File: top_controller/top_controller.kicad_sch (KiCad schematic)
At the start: 117 parts, among them J1 OUT1, J10 USB_C_Receptacle_USB2.0, J11 SWD, J12 UART, J13 BOOT0, J14 BOOT1, J2 OUT2, J3 OUT3, J4 OUT4, J5 OUT5, J6 OUT6, J7 OUT7, J8 OUT8, J9 PIN, SW1 RESET, U1 STM32F103C8Tx, U2 LT3045xMSE, U3 AD5754BREZ, U4 AD5754BREZ, U5 REF192, U6 EPM78V2, U7 REF192, Y1 8MHz

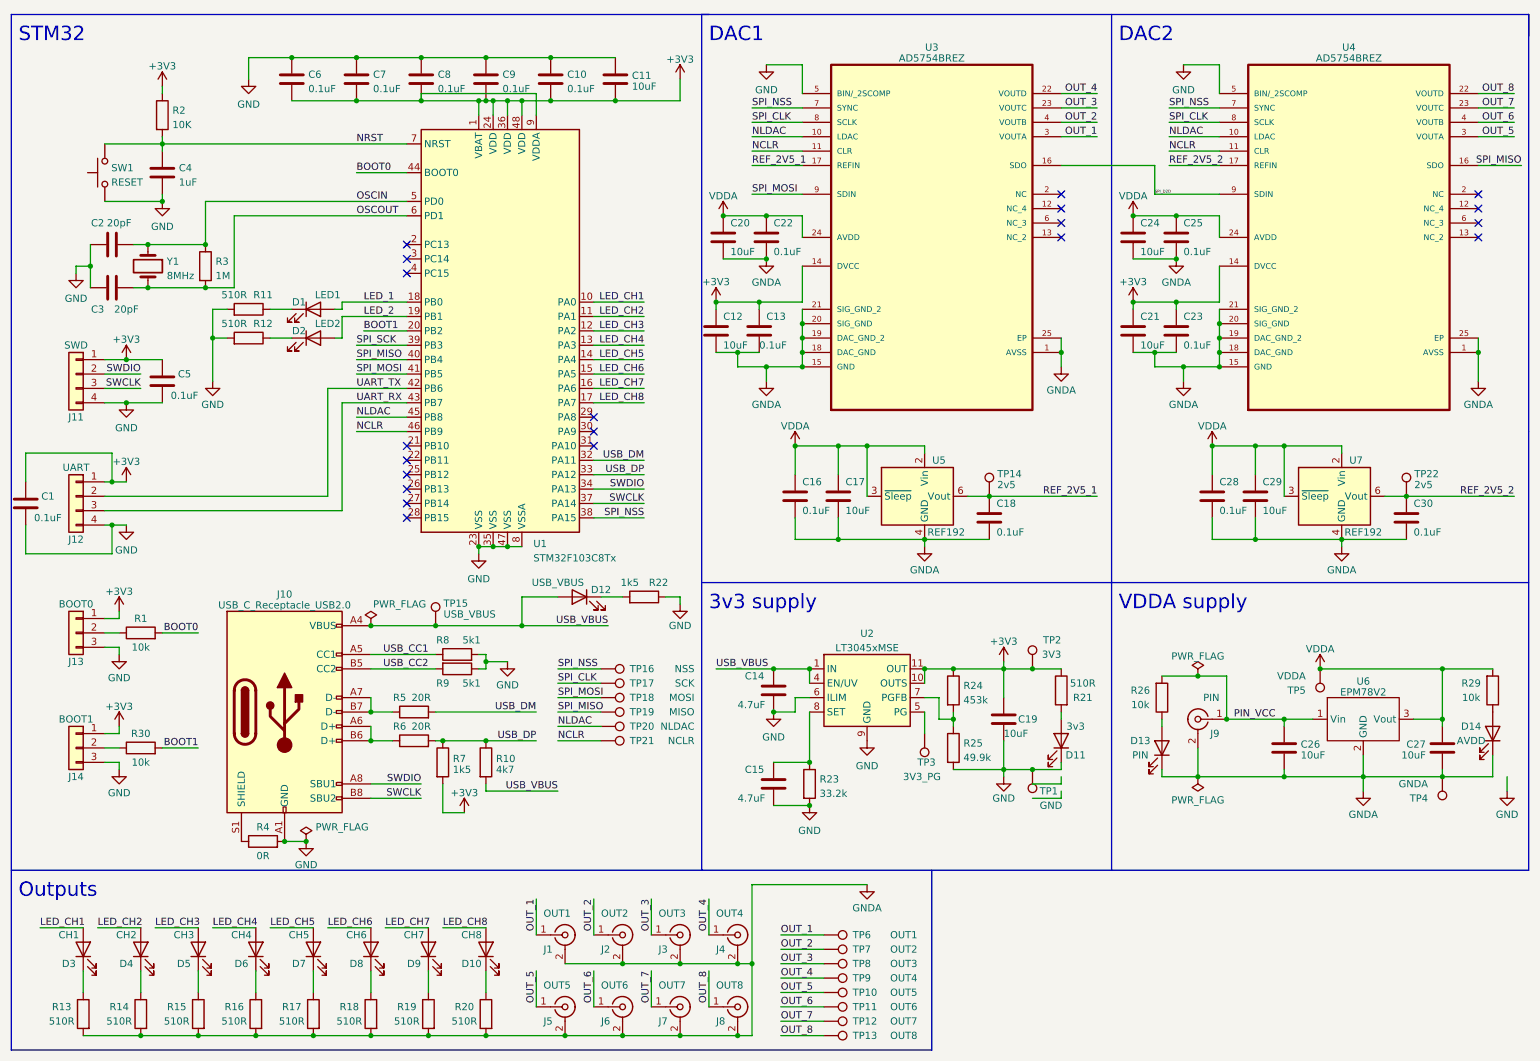
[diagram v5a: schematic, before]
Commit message: Reordered output channels on DACs for easier tracing
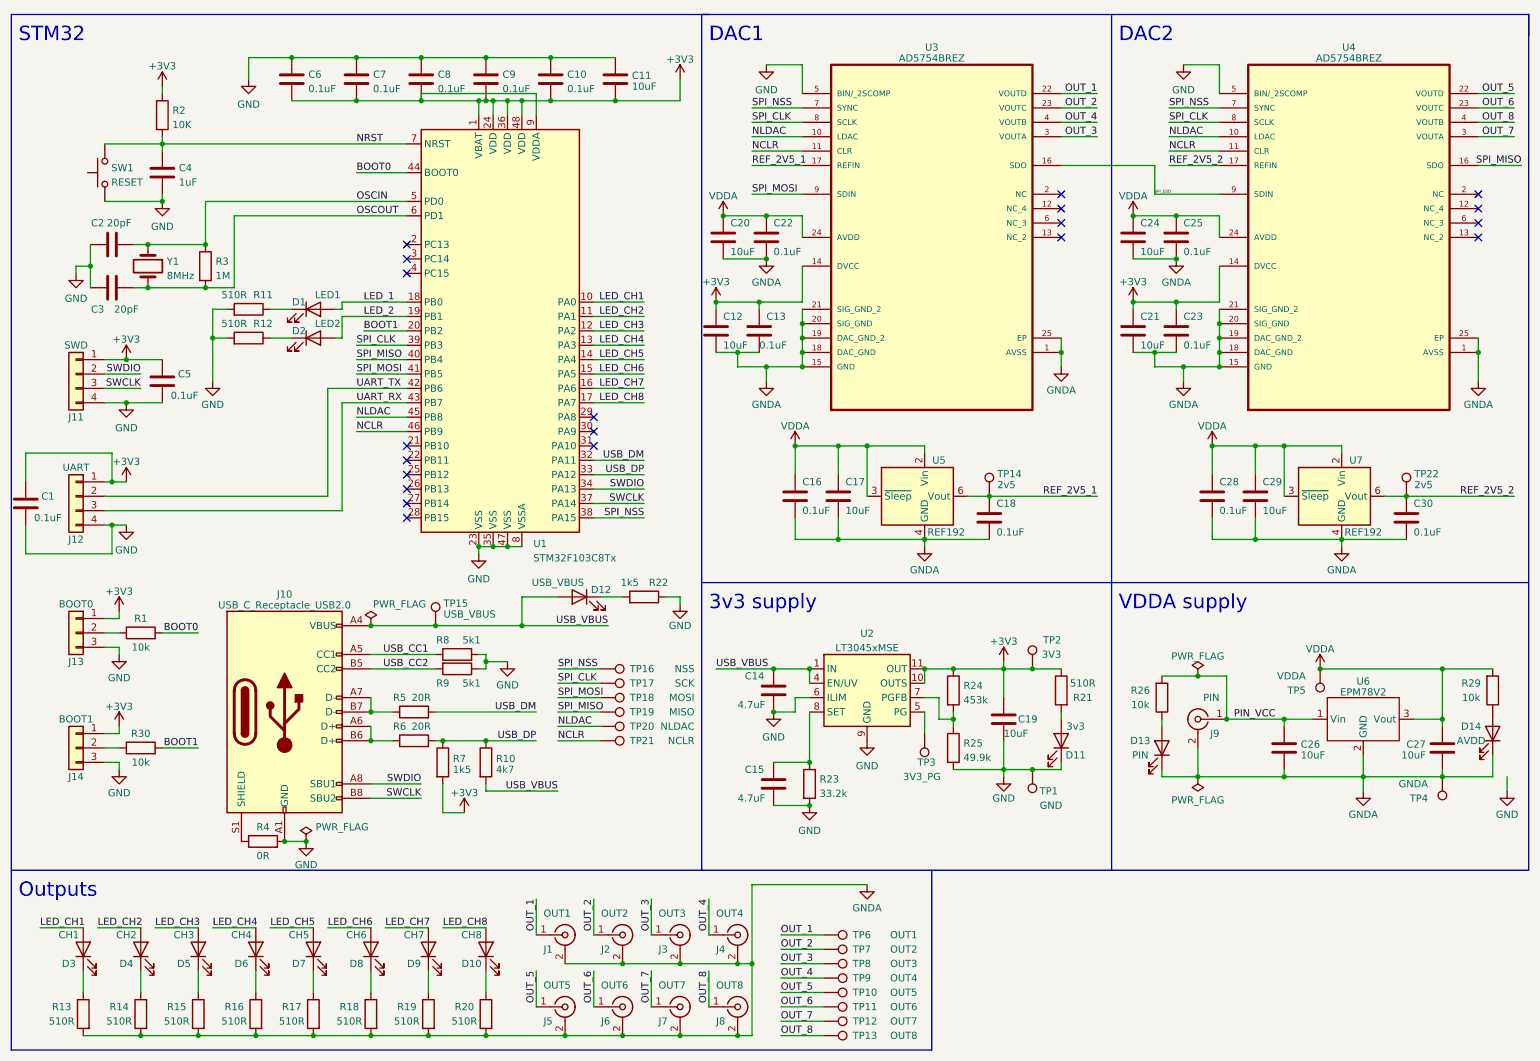
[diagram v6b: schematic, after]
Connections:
- net SPI_SCK is gone; now on net SPI_CLK: U1.39 (PB3)
- net OUT_1: now also U3.22 (VOUTD); no longer U3.3 (VOUTA)
- net OUT_2: now also U3.23 (VOUTC); no longer U3.4 (VOUTB)
- net OUT_3: now also U3.3 (VOUTA); no longer U3.23 (VOUTC)
- net OUT_4: now also U3.4 (VOUTB); no longer U3.22 (VOUTD)
- net OUT_5: now also U4.22 (VOUTD); no longer U4.3 (VOUTA)
- net OUT_6: now also U4.23 (VOUTC); no longer U4.4 (VOUTB)
- net OUT_7: now also U4.3 (VOUTA); no longer U4.23 (VOUTC)
- net OUT_8: now also U4.4 (VOUTB); no longer U4.22 (VOUTD)
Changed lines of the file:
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@@
-    (stroke (width 0) (type default))
-  )
-  (wire (pts (xy 199.39 149.86) (xy 194.31 149.86))
     (stroke (width 0) (type default))
   )
@@
     (stroke (width 0) (type default))
   )
-  (wire (pts (xy 199.39 152.4) (xy 194.31 152.4))
-    (stroke (width 0) (type default))
-  )
   (wire (pts (xy 199.39 71.12) (xy 199.39 73.66))
     (stroke (width 0) (type default))
@@
     (stroke (width 0) (type default))
   )
-  (wire (pts (xy 199.39 148.59) (xy 199.39 149.86))
-    (stroke (width 0) (type default))
-  )
   (wire (pts (xy 226.06 106.68) (xy 226.06 102.87))
     (stroke (width 0) (type default))
@@
     (stroke (width 0) (type default))
   )
-  (wire (pts (xy 199.39 151.13) (xy 199.39 152.4))
-    (stroke (width 0) (type default))
-  )
   (wire (pts (xy 149.86 191.77) (xy 157.48 191.77))
     (stroke (width 0) (type default))
@@
     (effects (font (size 1.27 1.27)) (justify right bottom))
   )
-  (label "OUT_1" (at 205.74 35.56 180) (fields_autoplaced)
+  (label "OUT_3" (at 205.74 35.56 180) (fields_autoplaced)
     (effects (font (size 1.27 1.27)) (justify right bottom))
   )
@@
     (effects (font (size 1.27 1.27)) (justify right bottom))
   )
-  (label "OUT_8" (at 279.4 27.94 180) (fields_autoplaced)
+  (label "OUT_5" (at 279.4 27.94 180) (fields_autoplaced)
     (effects (font (size 1.27 1.27)) (justify right bottom))
   )
@@
     (effects (font (size 1.27 1.27)) (justify left bottom))
   )
-  (label "OUT_7" (at 279.4 30.48 180) (fields_autoplaced)
+  (label "OUT_6" (at 279.4 30.48 180) (fields_autoplaced)
     (effects (font (size 1.27 1.27)) (justify right bottom))
   )
@@
     (effects (font (size 1.27 1.27)) (justify right bottom))
   )
-  (label "OUT_3" (at 205.74 30.48 180) (fields_autoplaced)
+  (label "OUT_2" (at 205.74 30.48 180) (fields_autoplaced)
     (effects (font (size 1.27 1.27)) (justify right bottom))
   )
@@
     (effects (font (size 1.27 1.27)) (justify left bottom))
   )
-  (label "SPI_SCK" (at 74.93 72.39 0) (fields_autoplaced)
-    (effects (font (size 1.27 1.27)) (justify left bottom))
-  )
-  (label "OUT_2" (at 205.74 33.02 180) (fields_autoplaced)
-    (effects (font (size 1.27 1.27)) (justify right bottom))
-  )
-  (label "OUT_4" (at 205.74 27.94 180) (fields_autoplaced)
+  (label "SPI_CLK" (at 74.93 72.39 0) (fields_autoplaced)
+    (effects (font (size 1.27 1.27)) (justify left bottom))
+  )
+  (label "OUT_4" (at 205.74 33.02 180) (fields_autoplaced)
+    (effects (font (size 1.27 1.27)) (justify right bottom))
+  )
+  (label "OUT_1" (at 205.74 27.94 180) (fields_autoplaced)
     (effects (font (size 1.27 1.27)) (justify right bottom))
   )
@@
     (effects (font (size 1.27 1.27)) (justify right bottom))
   )
-  (label "OUT_5" (at 279.4 35.56 180) (fields_autoplaced)
+  (label "OUT_7" (at 279.4 35.56 180) (fields_autoplaced)
     (effects (font (size 1.27 1.27)) (justify right bottom))
   )
@@
     (effects (font (size 1.27 1.27)) (justify left bottom))
   )
-  (label "OUT_6" (at 279.4 33.02 180) (fields_autoplaced)
-    (effects (font (size 1.27 1.27)) (justify right bottom))
-  )
+  (label "OUT_8" (at 279.4 33.02 180) (fields_autoplaced)
+    (effects (font (size 1.27 1.27)) (justify right bottom))
+  )

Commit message: Finished tracing - still some errors present
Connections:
- net GNDA is gone; now on net GND: C12.2, C13.2, C16.2, C17.2, C18.2, C20.2, C21.2, C22.2, C23.2, C24.2, C25.2, C26.2, C27.2, C28.2, C29.2, C30.2, D13.1 (K), D14.1 (K), J1.2 (Ext), J2.2 (Ext), J3.2 (Ext), J4.2 (Ext), J5.2 (Ext), J6.2 (Ext), J7.2 (Ext), J8.2 (Ext), J9.2 (Ext), R13.2, R14.2, R15.2, R16.2, R17.2, R18.2, R19.2, R20.2, TP4.1, U3.1 (AVSS), U3.15 (GND), U3.18 (DAC_GND), U3.19 (DAC_GND_2), U3.20 (SIG_GND), U3.21 (SIG_GND_2), U3.25 (EP), U4.1 (AVSS), U4.15 (GND), U4.18 (DAC_GND), U4.19 (DAC_GND_2), U4.20 (SIG_GND), U4.21 (SIG_GND_2), U4.25 (EP), U5.4 (GND), U6.2 (GND), U7.4 (GND)
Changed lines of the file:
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@@
   (junction (at 138.43 64.77) (diameter 0) (color 0 0 0 0)
+  )
+  (junction (at 275.59 148.59) (diameter 0) (color 0 0 0 0)
   )
   (junction (at 111.76 194.31) (diameter 0) (color 0 0 0 0)
@@
     (stroke (width 0) (type default))
   )
+  (wire (pts (xy 275.59 148.59) (xy 278.13 148.59))
+    (stroke (width 0) (type default))
+  )
